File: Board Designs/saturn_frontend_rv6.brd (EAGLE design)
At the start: 29 x 23.8 mm, 26 parts

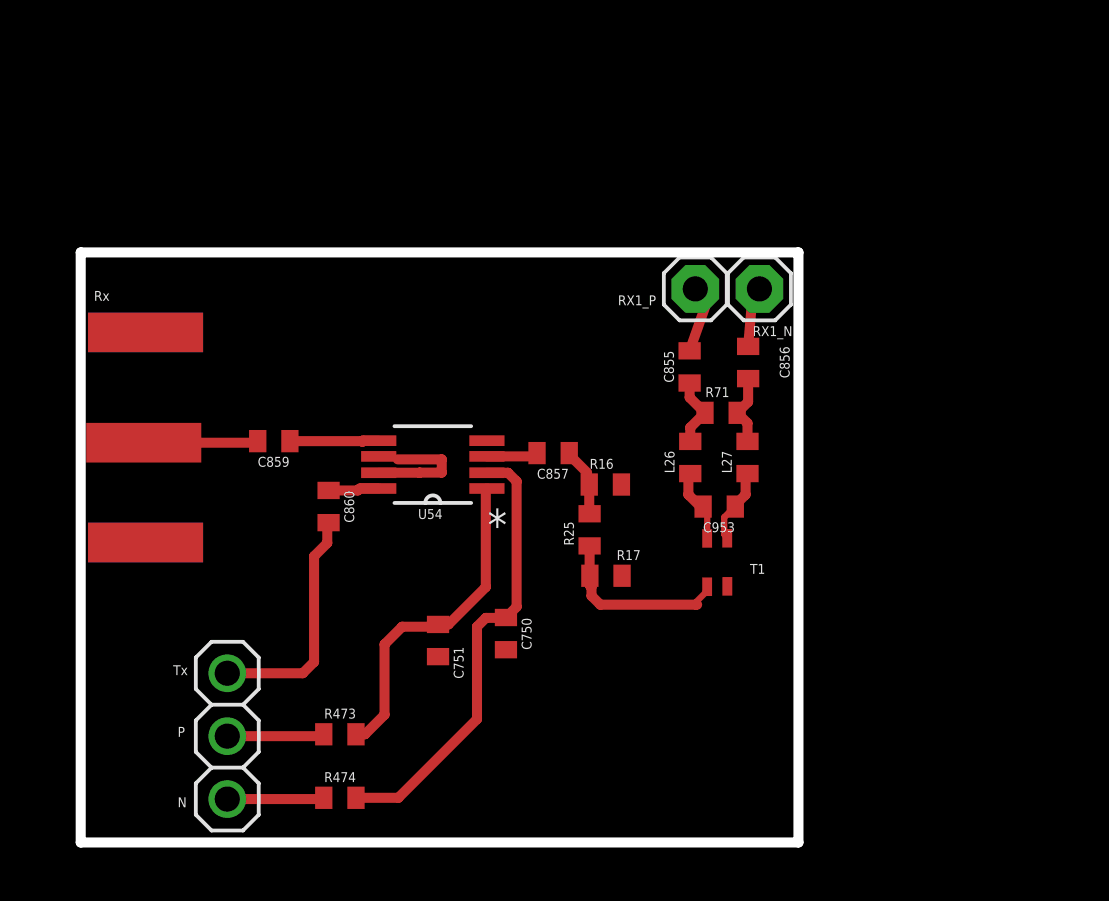
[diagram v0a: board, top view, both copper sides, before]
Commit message: added some scpi commands
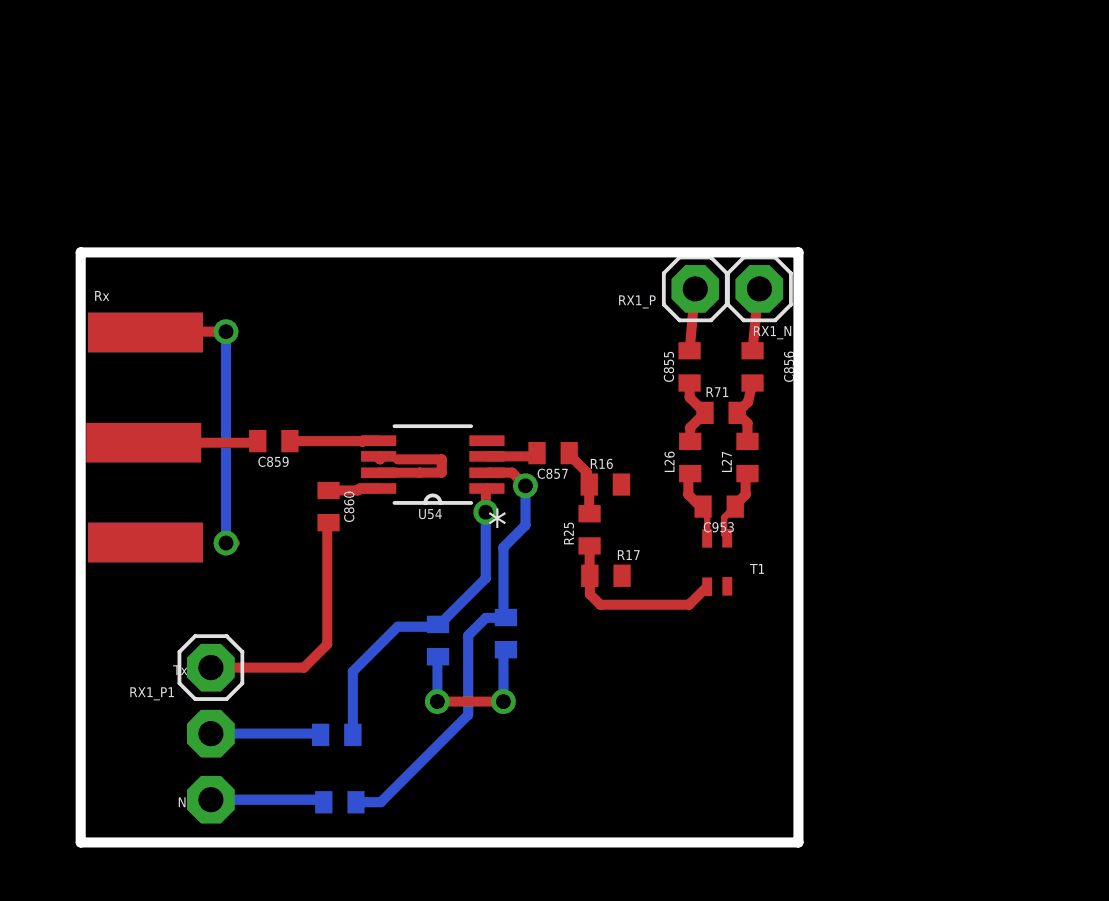
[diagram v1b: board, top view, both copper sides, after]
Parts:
- removed RX1_AUX: (no value), adafruit:1X03
- added RX1_P1, RX1_P2, RX1_P3: (no value), adafruit:1X01
- moved C856 0.25 mm to (38.9, 38.8)
- moved R474 0.18 mm to (22.2, 21.2), flipped to the bottom, turned to 180 degrees
- moved R473 0.13 mm to (22.1, 23.9), flipped to the bottom, turned to 180 degrees
- flipped C750 to the bottom
- flipped C751 to the bottom
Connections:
- net S$10 renamed S$32
- net S$8 renamed S$23
- net S$2: now also RX1_P1.1; no longer RX1_AUX.3
- net S$6: now also RX1_P2.1; no longer RX1_AUX.2
- net S$7: now also RX1_P3.1; no longer RX1_AUX.1
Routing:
- net GND: track 4.86 -> 24.1 mm, vias 0 -> 4
- net S$7: track 3.92 -> 4.74 mm
- net S$6: track 3.93 -> 4.45 mm
- net S$32: track 18.3 -> 18.5 mm, vias 0 -> 1
- net S$23: vias 0 -> 1

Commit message: Another Revision of the boards, with more sma connectors
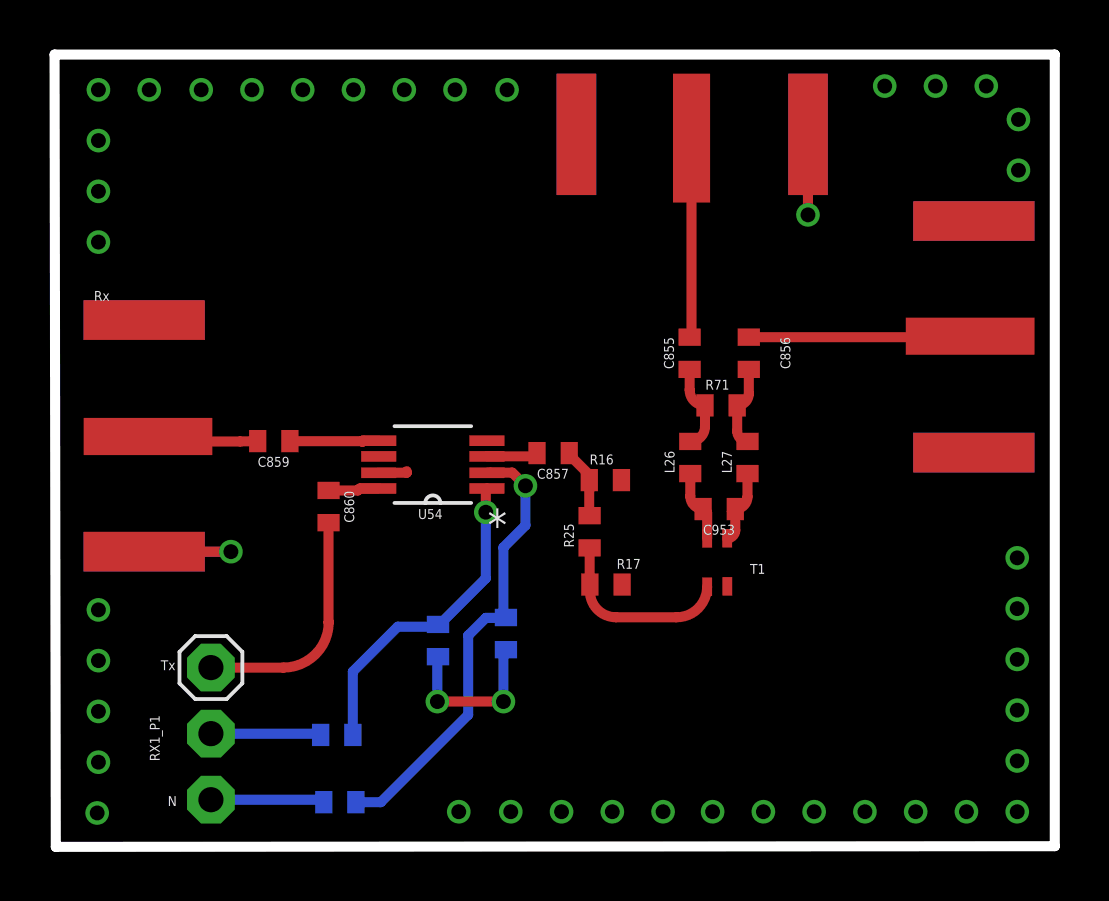
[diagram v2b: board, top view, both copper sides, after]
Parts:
- removed PAD1, PAD2, PAD4, PAD8113, PAD8114: (no value), project_1:PAD_0PRIMARY
- removed RX1_N, RX1_P: (no value), adafruit:1X01
- added E$2, E$3, E$4: (no value), cody_custom_library:SMA132289
- moved C856 0.57 mm to (38.7, 39.3)
- moved C855 0.55 mm to (36.3, 39.3)
- moved R17 0.36 mm to (32.9, 30.0)
- moved R71 0.30 mm to (37.6, 37.2)
- moved R16 0.18 mm to (32.9, 34.2)
- moved C953 0.10 mm to (37.5, 33.0)
- moved R25 0.08 mm to (32.3, 32.1)
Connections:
- net S$16 renamed S$10
- removed net S$18: C953.1, E$1.4, L27.1
- removed net S$27: C856.2, RX1_N.1
- new net S$33: C856.2, E$4.P$3
- new net S$34: C855.2, E$3.P$3
- new net S$8: E$1.1, R17.1, R25.1
- net GND: now also E$2.GND, E$2.P$1, E$2.P$2, E$2.P$5, E$3.GND, E$3.P$1, E$3.P$2, E$3.P$5, E$4.P$1, E$4.P$2, E$4.P$5; no longer PAD8113.1, PAD8114.1
- net S$1: no longer PAD4.1
- net S$14: no longer C857.1
- net S$25: now also C953.1, E$1.4, L27.1; no longer C855.2, RX1_P.1
- net S$28: now also C857.1; no longer E$1.1, R17.1, R25.1
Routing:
- net S$33: track 0.00 -> 8.98 mm
- net S$34: track 0.00 -> 8.12 mm
- net S$8: track 0.00 -> 7.60 mm
- net S$28: track 7.33 -> 1.09 mm
- net S$18: track 3.16 -> 0.00 mm, vias 0 -> 1
- net S$27: track 2.52 -> 0.00 mm, vias 0 -> 1
- net GND: track 24.1 -> 21.6 mm
- net S$14: track 2.85 -> 1.57 mm
- net S$25: track 2.51 -> 3.55 mm
- net S$1: track 4.63 -> 5.25 mm
- net S$10: track 2.86 -> 3.41 mm
- net S$19: track 2.73 -> 3.27 mm
- added copper zone on layer 16, net GND
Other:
- board size 29 x 23.8 mm -> 40.4 x 32 mm

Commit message: Next Revision of board
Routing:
- net GND: track 21.6 -> 73.1 mm, vias 4 -> 11
- added copper zone on layer 1, net SIGGND
- removed copper zone on layer 1, net GND
